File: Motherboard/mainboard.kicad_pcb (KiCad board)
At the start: 4 copper layers, 45.2 x 36 mm, 51 parts, among them IC1 BMX160, J1 Conn_01x01, J2 10118194-0001LF, J28 Conn_01x01, J29 Conn_01x01, J3 Micro_SD_Card, J30 Conn_01x01, J4 xf2m-2415-1a, J5 XF2M-1015-1A, J6 U.FL-R-SMT-1, J7 U.FL-R-SMT-1, J8 Conn_01x01, SW1 KMR231NG LFS, U1 RFM95W-915S2, U2 ATSAMD51G_TQFN48, U3 DRV8848, U4 TPS82740BSIPR, U5 DRV8848, U6 MAX708RESA-T, U8 RFM95W-915S2

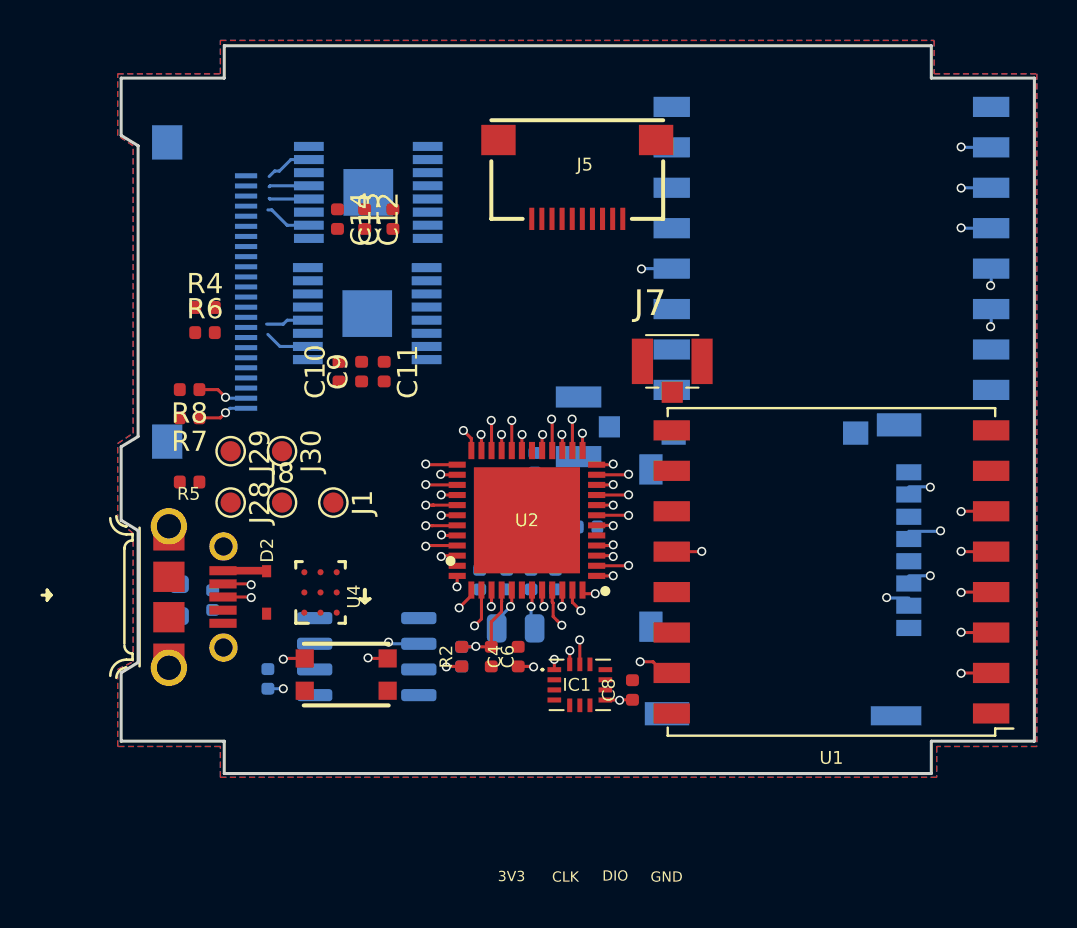
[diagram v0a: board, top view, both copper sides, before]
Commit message: routed except for connectors
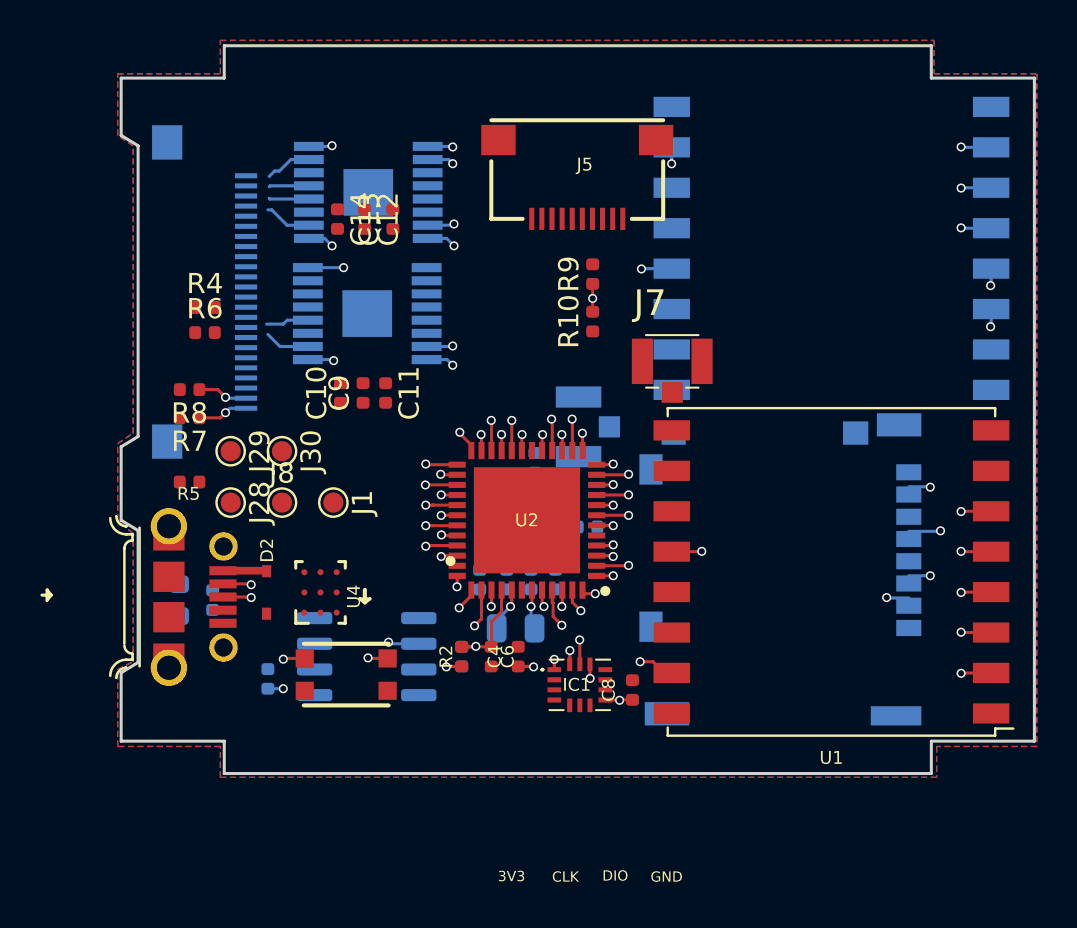
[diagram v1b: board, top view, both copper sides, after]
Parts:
- added R10: 100K, Resistor_SMD:R_0402_1005Metric, F.Cu at (99.9, 87.2)
- added R9: 100K, Resistor_SMD:R_0402_1005Metric, F.Cu at (99.9, 84.8)
- moved C10 1.06 mm to (87.5, 90.7)
- moved C11 1.06 mm to (89.7, 90.7)
- moved C9 1.06 mm to (88.6, 90.7)
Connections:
- J4 pad 11: BURN2 -> BATT_STATUS
- J4 pad 7: Net-(J4-Pad7) -> BURN2
- U2 pad 10: DAC1 -> BATTERY
- U2 pad 11: Net-(U2-Pad11) -> RF1_BUSY
- U2 pad 12: Net-(U2-Pad12) -> RF1_IO1
- U2 pad 16: Net-(U2-Pad16) -> EN_CAM
- U2 pad 19: Net-(U2-Pad19) -> CS_CAM
- U2 pad 20: Net-(U2-Pad20) -> MINZ_1
- U2 pad 21: Net-(U2-Pad21) -> MINZ_2
- U2 pad 22: Net-(U2-Pad22) -> MINX_2
- U2 pad 23: Net-(U2-Pad23) -> MINX_1
- U2 pad 24: Net-(U2-Pad24) -> MINY_1
- U2 pad 27: Net-(U2-Pad27) -> BATT_STATUS
- U2 pad 28: Net-(U2-Pad28) -> M_EN
- U2 pad 29: Net-(U2-Pad29) -> BURN2
- U2 pad 3: DAC0 -> RF2_IO1
- U2 pad 30: Net-(U2-Pad30) -> M_FAULT
- U2 pad 31: Net-(U2-Pad31) -> BURN1
- U2 pad 32: Net-(U2-Pad32) -> MINY_2
- U2 pad 7: TX -> RF2_RST
- U2 pad 8: RX -> RF1_RST
- U2 pad 9: Net-(U2-Pad9) -> RF1_CS
- U3 pad 1: MXZ_EN -> M_EN
- U3 pad 8: DXZ_FAULT -> M_FAULT
- U5 pad 1: MY_EN -> M_EN
- U5 pad 8: DY_FAULT -> M_FAULT
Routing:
- net M_FAULT: track 0.00 -> 24.8 mm, vias 0 -> 3
- net RF1_CS: track 0.85 -> 24.6 mm, vias 1 -> 2
- net RF1_RST: track 0.88 -> 24.0 mm, vias 1 -> 2
- net M_EN: track 0.00 -> 18.1 mm, vias 0 -> 3
- net Net-(U2-Pad24): track 17.8 -> 0.00 mm, vias 1 -> 0
- net RF1_IO1: track 0.00 -> 17.7 mm, vias 0 -> 2
- net MINZ_1: track 0.00 -> 17.5 mm, vias 0 -> 2
- net Net-(U2-Pad30): track 16.8 -> 0.00 mm, vias 1 -> 0
- net MINZ_2: track 0.00 -> 16.5 mm, vias 0 -> 2
- net Net-(U2-Pad19): track 16.4 -> 0.00 mm, vias 1 -> 0
- net Net-(U2-Pad20): track 15.5 -> 0.00 mm, vias 1 -> 0
- net BATT_STATUS: track 0.00 -> 15.4 mm, vias 0 -> 1
- net Net-(U2-Pad28): track 14.5 -> 0.00 mm, vias 1 -> 0
- net Net-(U2-Pad31): track 13.8 -> 0.00 mm, vias 1 -> 0
- net BURN1: track 0.00 -> 13.8 mm, vias 0 -> 1
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
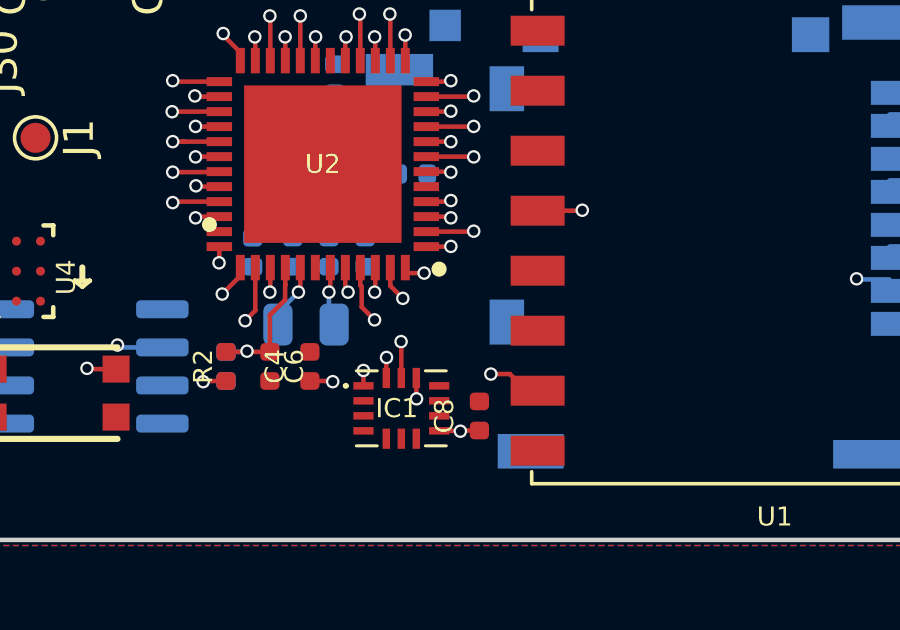
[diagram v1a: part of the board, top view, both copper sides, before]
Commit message: changed IMU from SPI to I2C for pins
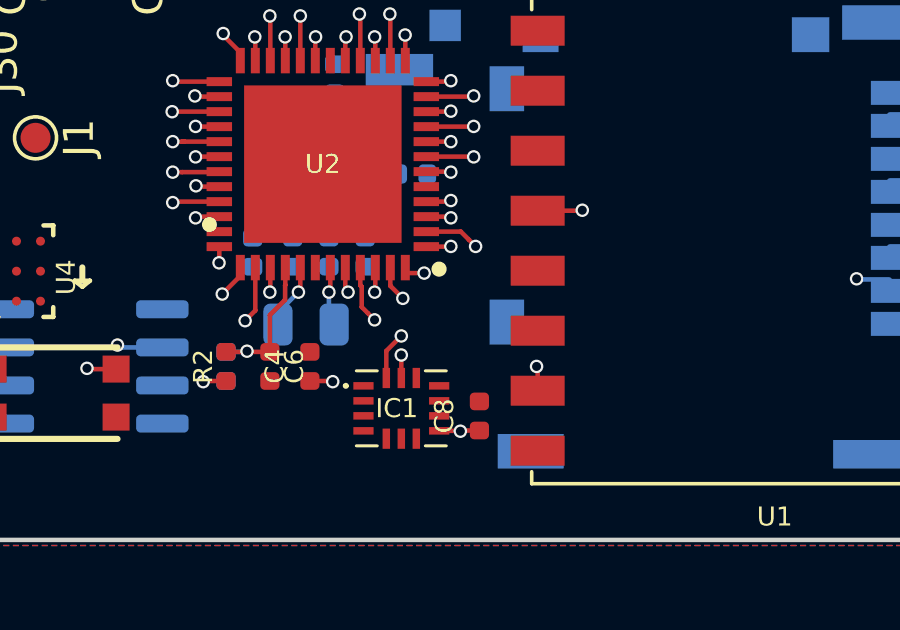
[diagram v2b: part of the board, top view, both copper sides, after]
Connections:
- IC1 pad 1: MISO -> Net-(IC1-Pad1)
- IC1 pad 12: CS_IMU -> +3V3
- IC1 pad 13: SCK -> SCL1
- IC1 pad 14: MOSI -> SDA1
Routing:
- net MISO: track 74.3 -> 42.1 mm, vias 5 -> 4
- net SCK: track 65.6 -> 33.5 mm, vias 5 -> 4
- net MOSI: track 69.1 -> 37.1 mm, vias 5 -> 4
- net SCL1: track 23.4 -> 29.3 mm, vias 1 -> 2
- net SDA1: track 21.9 -> 27.2 mm, vias 1 -> 2
- net CS_IMU: track 4.53 -> 0.00 mm, vias 1 -> 0

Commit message: lots of clean up
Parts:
- removed D1: GREEN, LED_SMD:LED_0603_1608Metric
- removed R1: 330, Resistor_SMD:R_0402_1005Metric
- added D3: WS2812B, LED_SMD:LED_WS2812B_PLCC4_5.0x5.0mm_P3.2mm, B.Cu at (81.5, 100.8)
- moved R3 7.57 mm to (86.0, 104.8)
- moved C12 5.91 mm to (88.6, 76.2)
- moved C13 5.91 mm to (90.0, 76.2)
- moved C14 5.91 mm to (87.3, 76.2)
- moved J6 3.45 mm to (100.0, 89.0), turned to 180 degrees
- moved J5 2.79 mm to (100.3, 79.6)
- moved R4 2.11 mm to (79.4, 88.1)
- moved R6 2.11 mm to (79.4, 89.3)
- moved U6 1.45 mm to (89.9, 102.9), turned to 270 degrees
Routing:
- net (no net): track 0.00 -> 30.2 mm, vias 0 -> 4
- net SCK: track 33.5 -> 55.1 mm
- net MOSI: track 37.1 -> 57.1 mm
- net MISO: track 42.1 -> 59.1 mm
- net GND: track 0.76 -> 9.84 mm, vias 1 -> 19
- net BATT_P: track 7.73 -> 0.00 mm
- net ~RESET: track 17.3 -> 21.2 mm, vias 3 -> 2
- net Net-(R3-Pad2): track 0.00 -> 3.35 mm
- net BATT_STATUS: track 15.4 -> 12.8 mm
- net MOX_2: track 1.98 -> 4.49 mm, vias 0 -> 1
- net MOZ_2: track 1.98 -> 4.49 mm, vias 0 -> 2
- net MOY_1: track 2.22 -> 4.45 mm, vias 0 -> 2
- net MOX_1: track 2.34 -> 4.55 mm, vias 0 -> 1
- net MOY_2: track 2.12 -> 4.25 mm, vias 0 -> 2
- net MOZ_1: track 2.31 -> 4.34 mm, vias 0 -> 2
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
